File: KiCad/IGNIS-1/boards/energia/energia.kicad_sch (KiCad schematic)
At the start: 4 parts, among them J40 Backplane, U3 Boost_5V

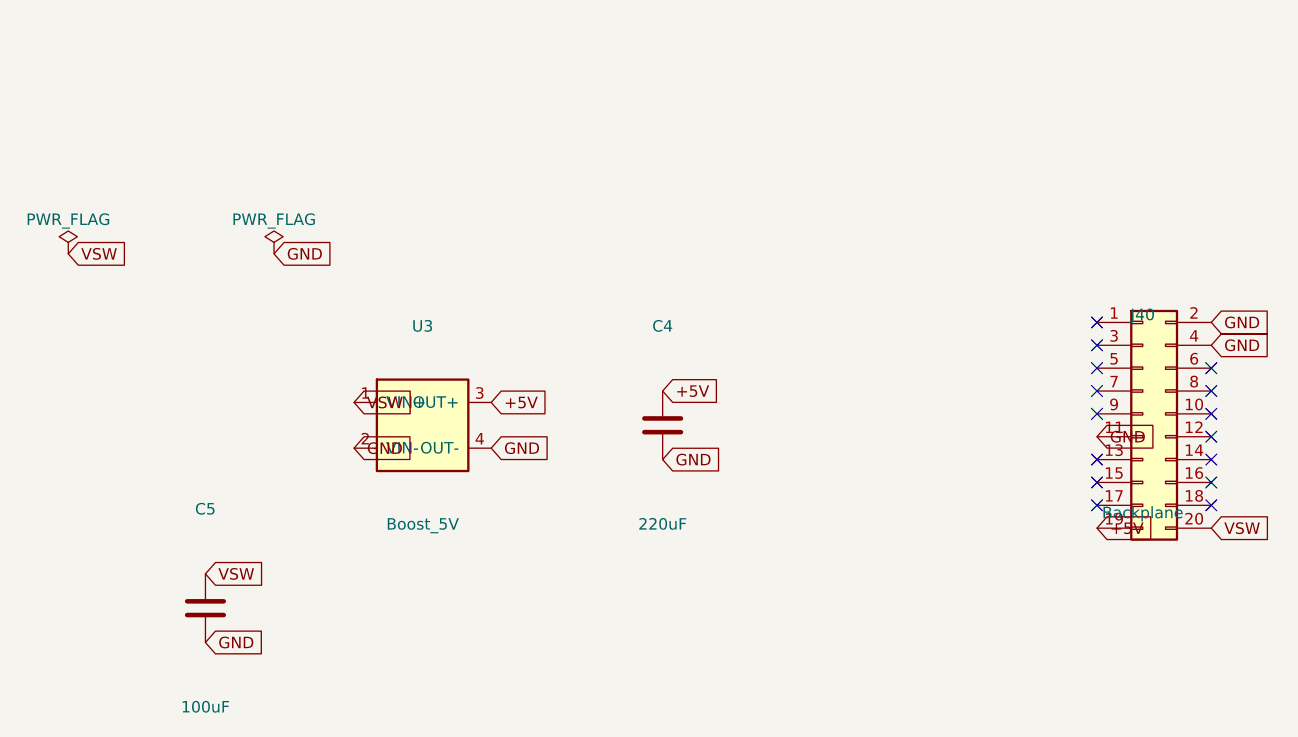
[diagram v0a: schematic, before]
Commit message: wip: recableo backplane split en progreso (GUI) + doc con move TPS63020
Co-Authored-By: Claude Opus 4.8 <noreply@anthropic.com>
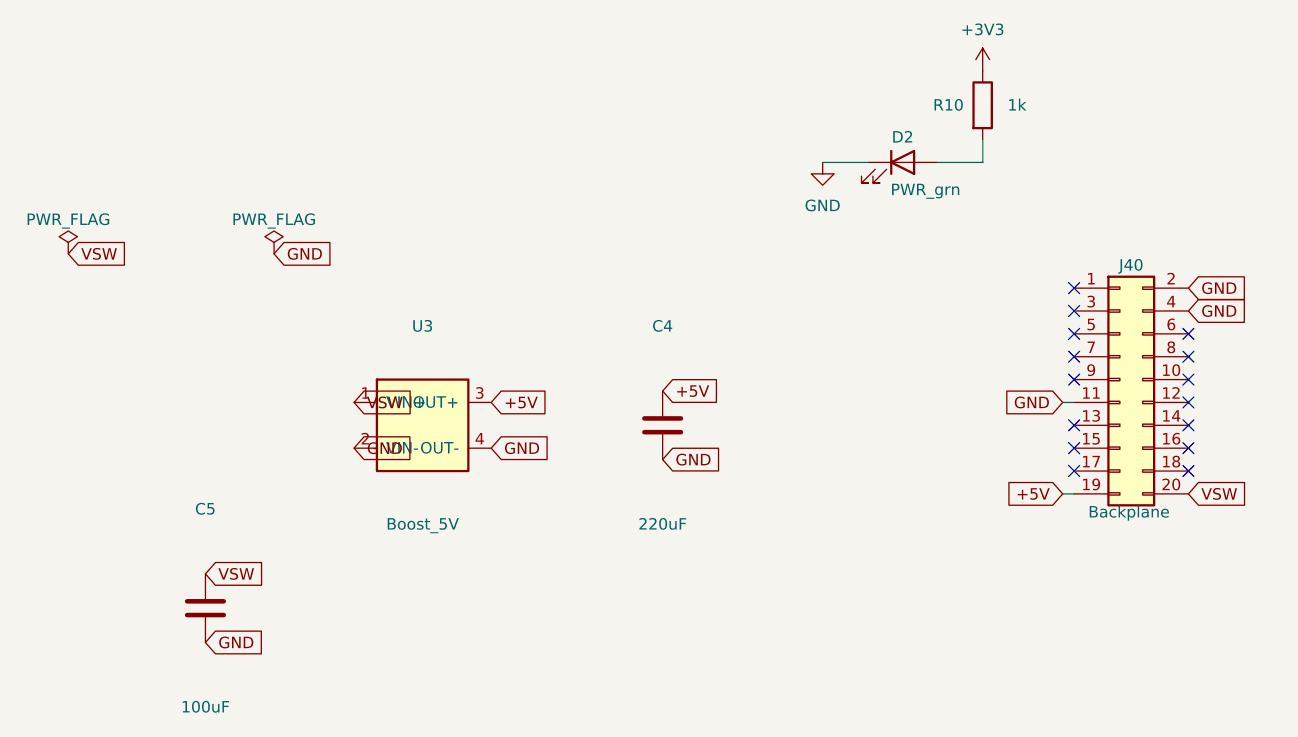
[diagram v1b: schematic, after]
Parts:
- added D2: PWR_grn, LED_THT:LED_D3.0mm, symbol Device:LED
- added R10: 1k, Resistor_THT:R_Axial_DIN0207_L6.3mm_D2.5mm_P7.62mm_Horizontal, symbol Device:R
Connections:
- net GND: now also D2.1 (K)
- new net: D2.2 (A), R10.2
- new net +3V3: R10.1
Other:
- moved on the sheet: J40
